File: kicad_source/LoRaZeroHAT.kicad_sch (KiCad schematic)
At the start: 5 parts

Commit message: glued project together
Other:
- removed sheet RP2040
- added sheet RaspberryPiZeroHAT (RaspberryPiZeroHAT.kicad_sch)
- title: RP2040LoRaTracker -> LoRaZeroHAT
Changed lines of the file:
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@@
 	(paper "A4")
 	(title_block
-		(title "RP2040LoRaTracker")
-		(date "2025-05-04")
+		(title "LoRaZeroHAT")
+		(date "2025-09-02")
 		(rev "0.1")
 		(company "generationmake")
@@
 	)
 	(sheet
-		(at 215.9 114.3)
+		(at 215.9 151.13)
 		(size 22.86 10.16)
 		(fields_autoplaced yes)
@@
 			(color 0 0 0 0.0000)
 		)
-		(property "Sheetname" "RP2040"
-			(at 215.9 113.5884 0)
+		(property "Sheetname" "RaspberryPiZeroHAT"
+			(at 215.9 150.4184 0)
 			(effects
 				(font
@@
 			)
 		)
-		(property "Sheetfile" "RP2040.kicad_sch"
-			(at 215.9 125.0446 0)
+		(property "Sheetfile" "RaspberryPiZeroHAT.kicad_sch"
+			(at 215.9 161.8746 0)
 			(effects
 				(font
@@
 		)
 		(instances
-			(project "RP2040LoRaTracker"
-				(path "/143f7a5b-9016-4d2c-b741-f535648590f8"
-					(page "2")
+			(project "LoRaZeroHAT"
+				(path "/143f7a5b-9016-4d2c-b741-f535648590f8"
+					(page "4")
 				)
 			)
@@
 		)
 		(instances
-			(project "RP2040LoRaTracker"
+			(project "LoRaZeroHAT"
 				(path "/143f7a5b-9016-4d2c-b741-f535648590f8"
 					(page "3")

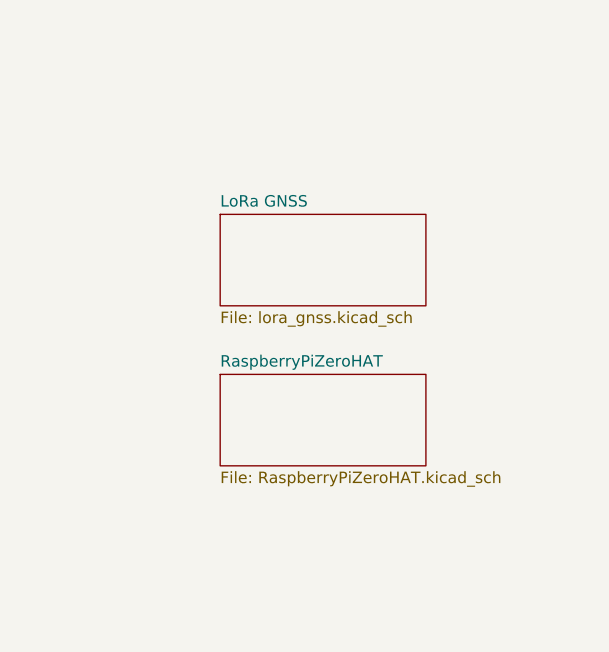
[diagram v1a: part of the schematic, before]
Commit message: connected schematic to layout
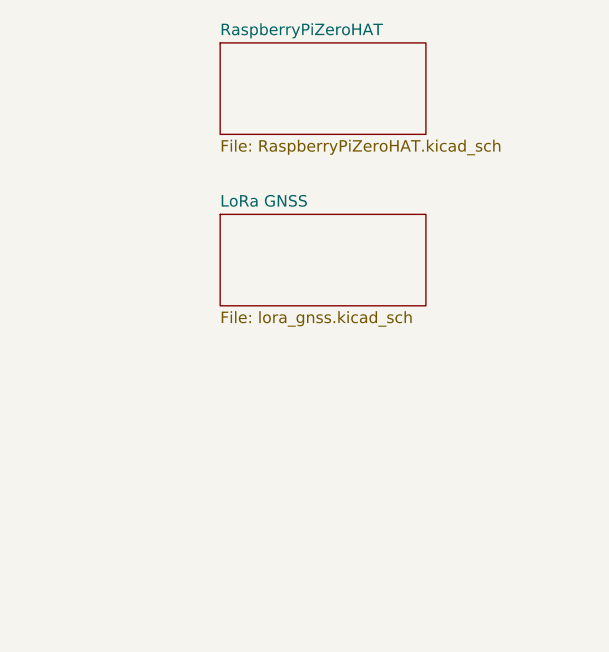
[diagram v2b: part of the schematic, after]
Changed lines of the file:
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@@
 	)
 	(sheet
-		(at 215.9 151.13)
+		(at 215.9 114.3)
 		(size 22.86 10.16)
 		(fields_autoplaced yes)
@@
 		)
 		(property "Sheetname" "RaspberryPiZeroHAT"
-			(at 215.9 150.4184 0)
+			(at 215.9 113.5884 0)
 			(effects
 				(font
@@
 		)
 		(property "Sheetfile" "RaspberryPiZeroHAT.kicad_sch"
-			(at 215.9 161.8746 0)
+			(at 215.9 125.0446 0)
 			(effects
 				(font
@@
 			(project "LoRaZeroHAT"
 				(path "/143f7a5b-9016-4d2c-b741-f535648590f8"
-					(page "4")
+					(page "2")
 				)
 			)

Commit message: made first connections
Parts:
- removed H1, H2, H3: MountingHole, MountingHole:MountingHole_2.2mm_M2, symbol Mechanical:MountingHole
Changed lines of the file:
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@@
-	)
-	(symbol
-		(lib_id "Mechanical:MountingHole")
-		(at 25.4 175.26 0)
-		(unit 1)
-		(exclude_from_sim yes)
-		(in_bom no)
-		(on_board yes)
-		(dnp no)
-		(fields_autoplaced yes)
-		(property "Reference" "H1"
-			(at 27.94 173.9899 0)
-			(effects
-				(font
-					(size 1.27 1.27)
-				)
-				(justify left)
-			)
-		)
-		(property "Value" "MountingHole"
-			(at 27.94 176.5299 0)
-			(effects
-				(font
-					(size 1.27 1.27)
-				)
-				(justify left)
-			)
-		)
-		(property "Footprint" "MountingHole:MountingHole_2.2mm_M2"
-			(at 25.4 175.26 0)
-			(effects
-				(font
-					(size 1.27 1.27)
-				)
-				(hide yes)
-			)
-		)
-		(property "Datasheet" "~"
-			(at 25.4 175.26 0)
-			(effects
-				(font
-					(size 1.27 1.27)
-				)
-				(hide yes)
-			)
-		)
-		(property "Description" "Mounting Hole without connection"
-			(at 25.4 175.26 0)
-			(effects
-				(font
-					(size 1.27 1.27)
-				)
-				(hide yes)
-			)
-		)
-		(instances
-			(project ""
-				(path "/143f7a5b-9016-4d2c-b741-f535648590f8"
-					(reference "H1")
-					(unit 1)
-				)
-			)
-		)
-	)
-	(symbol
-		(lib_id "Mechanical:MountingHole")
-		(at 25.4 181.61 0)
-		(unit 1)
-		(exclude_from_sim yes)
-		(in_bom no)
-		(on_board yes)
-		(dnp no)
-		(fields_autoplaced yes)
-		(property "Reference" "H2"
-			(at 27.94 180.3399 0)
-			(effects
-				(font
-					(size 1.27 1.27)
-				)
-				(justify left)
-			)
-		)
-		(property "Value" "MountingHole"
-			(at 27.94 182.8799 0)
-			(effects
-				(font
-					(size 1.27 1.27)
-				)
-				(justify left)
-			)
-		)
-		(property "Footprint" "MountingHole:MountingHole_2.2mm_M2"
-			(at 25.4 181.61 0)
-			(effects
-				(font
-					(size 1.27 1.27)
-				)
-				(hide yes)
-			)
-		)
-		(property "Datasheet" "~"
-			(at 25.4 181.61 0)
-			(effects
-				(font
-					(size 1.27 1.27)
-				)
-				(hide yes)
-			)
-		)
-		(property "Description" "Mounting Hole without connection"
-			(at 25.4 181.61 0)
-			(effects
-				(font
-					(size 1.27 1.27)
-				)
-				(hide yes)
-			)
-		)
-		(instances
-			(project "RP2040LoRaTracker"
-				(path "/143f7a5b-9016-4d2c-b741-f535648590f8"
-					(reference "H2")
-					(unit 1)
-				)
-			)
-		)
-	)
-	(symbol
-		(lib_id "Mechanical:MountingHole")
-		(at 25.4 187.96 0)
-		(unit 1)
-		(exclude_from_sim yes)
-		(in_bom no)
-		(on_board yes)
-		(dnp no)
-		(fields_autoplaced yes)
-		(property "Reference" "H3"
-			(at 27.94 186.6899 0)
-			(effects
-				(font
-					(size 1.27 1.27)
-				)
-				(justify left)
-			)
-		)
-		(property "Value" "MountingHole"
-			(at 27.94 189.2299 0)
-			(effects
-				(font
-					(size 1.27 1.27)
-				)
-				(justify left)
-			)
-		)
-		(property "Footprint" "MountingHole:MountingHole_2.2mm_M2"
-			(at 25.4 187.96 0)
-			(effects
-				(font
-					(size 1.27 1.27)
-				)
-				(hide yes)
-			)
-		)
-		(property "Datasheet" "~"
-			(at 25.4 187.96 0)
-			(effects
-				(font
-					(size 1.27 1.27)
-				)
-				(hide yes)
-			)
-		)
-		(property "Description" "Mounting Hole without connection"
-			(at 25.4 187.96 0)
-			(effects
-				(font
-					(size 1.27 1.27)
-				)
-				(hide yes)
-			)
-		)
-		(instances
-			(project "RP2040LoRaTracker"
-				(path "/143f7a5b-9016-4d2c-b741-f535648590f8"
-					(reference "H3")
-					(unit 1)
-				)
-			)
-		)
 	)
 	(symbol

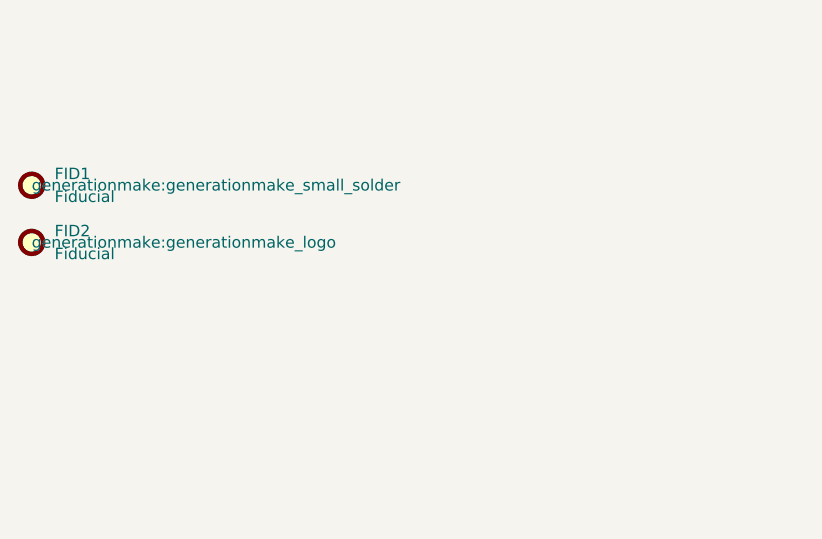
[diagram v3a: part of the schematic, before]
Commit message: updated layout
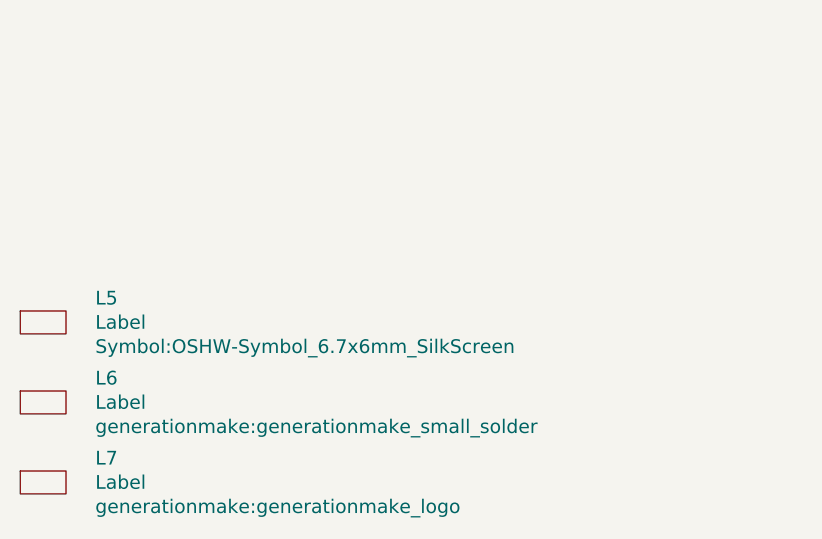
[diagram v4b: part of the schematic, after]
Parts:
- removed FID1: Fiducial, generationmake:generationmake_small_solder, symbol Mechanical:Fiducial
- removed FID2: Fiducial, generationmake:generationmake_logo, symbol Mechanical:Fiducial
- added L5: Label, Symbol:OSHW-Symbol_6.7x6mm_SilkScreen, symbol generationmake:Label
- added L6: Label, generationmake:generationmake_small_solder, symbol generationmake:Label
- added L7: Label, generationmake:generationmake_logo, symbol generationmake:Label
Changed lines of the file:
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@@
 	)
 	(symbol
-		(lib_id "Mechanical:Fiducial")
-		(at 25.4 156.21 0)
+		(lib_id "generationmake:Label")
+		(at 26.67 171.45 0)
 		(unit 1)
-		(exclude_from_sim yes)
+		(exclude_from_sim no)
 		(in_bom no)
 		(on_board yes)
 		(dnp no)
-		(fields_autoplaced yes)
-		(property "Reference" "FID1"
-			(at 27.94 154.9399 0)
+		(property "Reference" "L5"
+			(at 32.4612 168.7576 0)
 			(effects
 				(font
-					(size 1.27 1.27)
+					(size 1.524 1.524)
 				)
 				(justify left)
 			)
 		)
-		(property "Value" "Fiducial"
-			(at 27.94 157.4799 0)
+		(property "Value" "Label"
+			(at 32.4612 171.45 0)
 			(effects
 				(font
-					(size 1.27 1.27)
+					(size 1.524 1.524)
 				)
 				(justify left)
 			)
 		)
-		(property "Footprint" "generationmake:generationmake_small_solder"
-			(at 25.4 156.21 0)
+		(property "Footprint" "Symbol:OSHW-Symbol_6.7x6mm_SilkScreen"
+			(at 32.4612 174.1424 0)
 			(effects
 				(font
-					(size 1.27 1.27)
+					(size 1.524 1.524)
 				)
 				(justify left)
 			)
 		)
-		(property "Datasheet" "~"
-			(at 25.4 156.21 0)
+		(property "Datasheet" ""
+			(at 26.67 171.45 0)
 			(effects
 				(font
-					(size 1.27 1.27)
+					(size 1.524 1.524)
 				)
-				(hide yes)
 			)
 		)
-		(property "Description" "Fiducial Marker"
-			(at 25.4 156.21 0)
+		(property "Description" ""
+			(at 26.67 171.45 0)
 			(effects
 				(font
@@
 		)
 		(instances
-			(project ""
+			(project "LoRaZeroHAT"
 				(path "/143f7a5b-9016-4d2c-b741-f535648590f8"
-					(reference "FID1")
+					(reference "L5")
 					(unit 1)
 				)
@@
 	)
 	(symbol
-		(lib_id "Mechanical:Fiducial")
-		(at 25.4 162.56 0)
+		(lib_id "generationmake:Label")
+		(at 26.67 180.34 0)
 		(unit 1)
-		(exclude_from_sim yes)
+		(exclude_from_sim no)
 		(in_bom no)
 		(on_board yes)
 		(dnp no)
-		(fields_autoplaced yes)
-		(property "Reference" "FID2"
-			(at 27.94 161.2899 0)
+		(property "Reference" "L6"
+			(at 32.4612 177.6476 0)
 			(effects
 				(font
-					(size 1.27 1.27)
+					(size 1.524 1.524)
 				)
 				(justify left)
 			)
 		)
-		(property "Value" "Fiducial"
-			(at 27.94 163.8299 0)
+		(property "Value" "Label"
+			(at 32.4612 180.34 0)
 			(effects
 				(font
-					(size 1.27 1.27)
+					(size 1.524 1.524)
 				)
 				(justify left)
 			)
 		)
-		(property "Footprint" "generationmake:generationmake_logo"
-			(at 25.4 162.56 0)
+		(property "Footprint" "generationmake:generationmake_small_solder"
+			(at 32.4612 183.0324 0)
 			(effects
 				(font
-					(size 1.27 1.27)
+					(size 1.524 1.524)
 				)
 				(justify left)
 			)
 		)
-		(property "Datasheet" "~"
-			(at 25.4 162.56 0)
+		(property "Datasheet" ""
+			(at 26.67 180.34 0)
 			(effects
 				(font
-					(size 1.27 1.27)
+					(size 1.524 1.524)
 				)
-				(hide yes)
 			)
 		)
-		(property "Description" "Fiducial Marker"
-			(at 25.4 162.56 0)
+		(property "Description" ""
+			(at 26.67 180.34 0)
 			(effects
 				(font
@@
 		)
 		(instances
-			(project "RP2040LoRaTracker"
+			(project "LoRaZeroHAT"
 				(path "/143f7a5b-9016-4d2c-b741-f535648590f8"
-					(reference "FID2")
+					(reference "L6")
 					(unit 1)
 				)
+			)
+		)
+	)
+	(symbol
+		(lib_id "generationmake:Label")
+		(at 26.67 189.23 0)
+		(unit 1)
+		(exclude_from_sim no)
+		(in_bom no)
+		(on_board yes)
+		(dnp no)
+		(property "Reference" "L7"
+			(at 32.4612 186.5376 0)
+			(effects
+				(font
+					(size 1.524 1.524)
+				)
+				(justify left)
+			)
+		)
+		(property "Value" "Label"
+			(at 32.4612 189.23 0)
+			(effects
+				(font
+					(size 1.524 1.524)
+				)
+				(justify left)
+			)
+		)
+		(property "Footprint" "generationmake:generationmake_logo"
+			(at 32.4612 191.9224 0)
+			(effects
+				(font
+					(size 1.524 1.524)
+				)
+				(justify left)
+			)
+		)
+		(property "Datasheet" ""
+			(at 26.67 189.23 0)
+			(effects
+				(font
+					(size 1.524 1.524)
+				)
+			)
+		)
+		(property "Description" ""
+			(at 26.67 189.23 0)
+			(effects
+				(font
+					(size 1.27 1.27)
+				)
+				(hide yes)
+			)
+		)
+		(instances
+			(project "LoRaZeroHAT"
+				(path "/143f7a5b-9016-4d2c-b741-f535648590f8"
+					(reference "L7")
+					(unit 1)
+				)

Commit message: schaltplan neu annotiert
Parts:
- renumbered L5 to L1, L6 to L2, L7 to L3
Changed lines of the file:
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@@
 		(on_board yes)
 		(dnp no)
-		(property "Reference" "L5"
+		(property "Reference" "L1"
 			(at 32.4612 168.7576 0)
 			(effects
@@
 			(project "LoRaZeroHAT"
 				(path "/143f7a5b-9016-4d2c-b741-f535648590f8"
-					(reference "L5")
+					(reference "L1")
 					(unit 1)
 				)
@@
 		(on_board yes)
 		(dnp no)
-		(property "Reference" "L6"
+		(property "Reference" "L2"
 			(at 32.4612 177.6476 0)
 			(effects
@@
 			(project "LoRaZeroHAT"
 				(path "/143f7a5b-9016-4d2c-b741-f535648590f8"
-					(reference "L6")
+					(reference "L2")
 					(unit 1)
 				)
@@
 		(on_board yes)
 		(dnp no)
-		(property "Reference" "L7"
+		(property "Reference" "L3"
 			(at 32.4612 186.5376 0)
 			(effects
@@
 			(project "LoRaZeroHAT"
 				(path "/143f7a5b-9016-4d2c-b741-f535648590f8"
-					(reference "L7")
+					(reference "L3")
 					(unit 1)
 				)
